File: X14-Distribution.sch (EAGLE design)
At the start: 57 parts, among them Q1 310mA/60V/1.6Ω, Q2 IRF1018EPBF, Q3 IRF1018EPBF, Q4 IRF1018EPBF, Q5 310mA/60V/1.6Ω, Q6 310mA/60V/1.6Ω, Q7 310mA/60V/1.6Ω, Q8 310mA/60V/1.6Ω, U1 DIST_OR_CONTROL_ALTMK06A-M, U2 DIST_OR_CONTROL_ALTMK06A-M

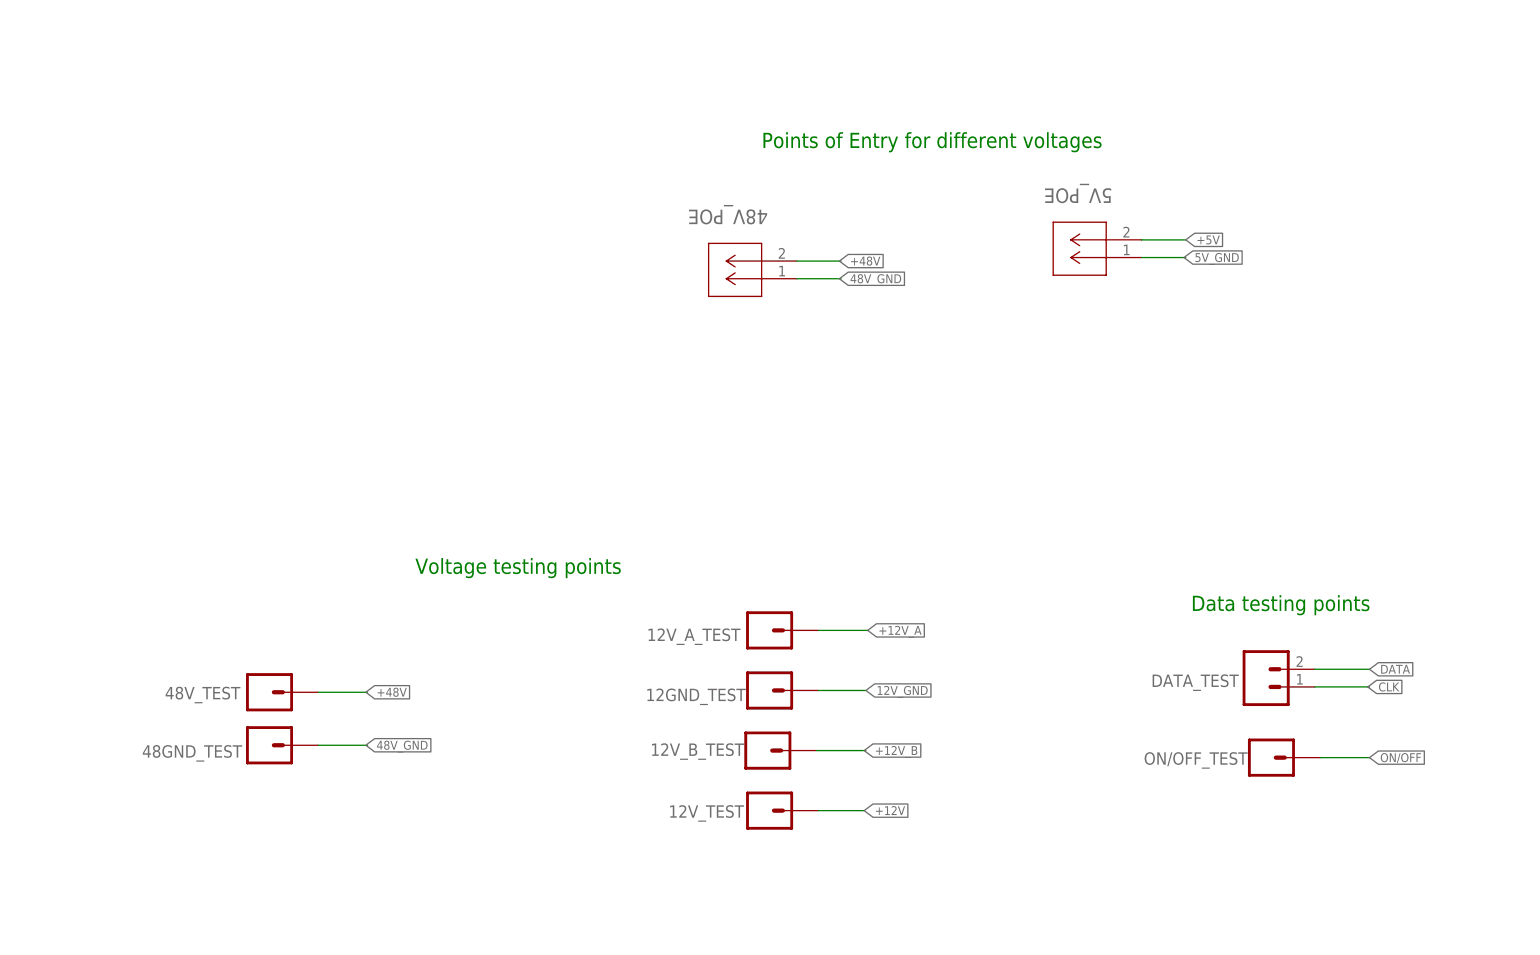
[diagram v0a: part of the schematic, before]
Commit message: Changed footprint of schottky diode
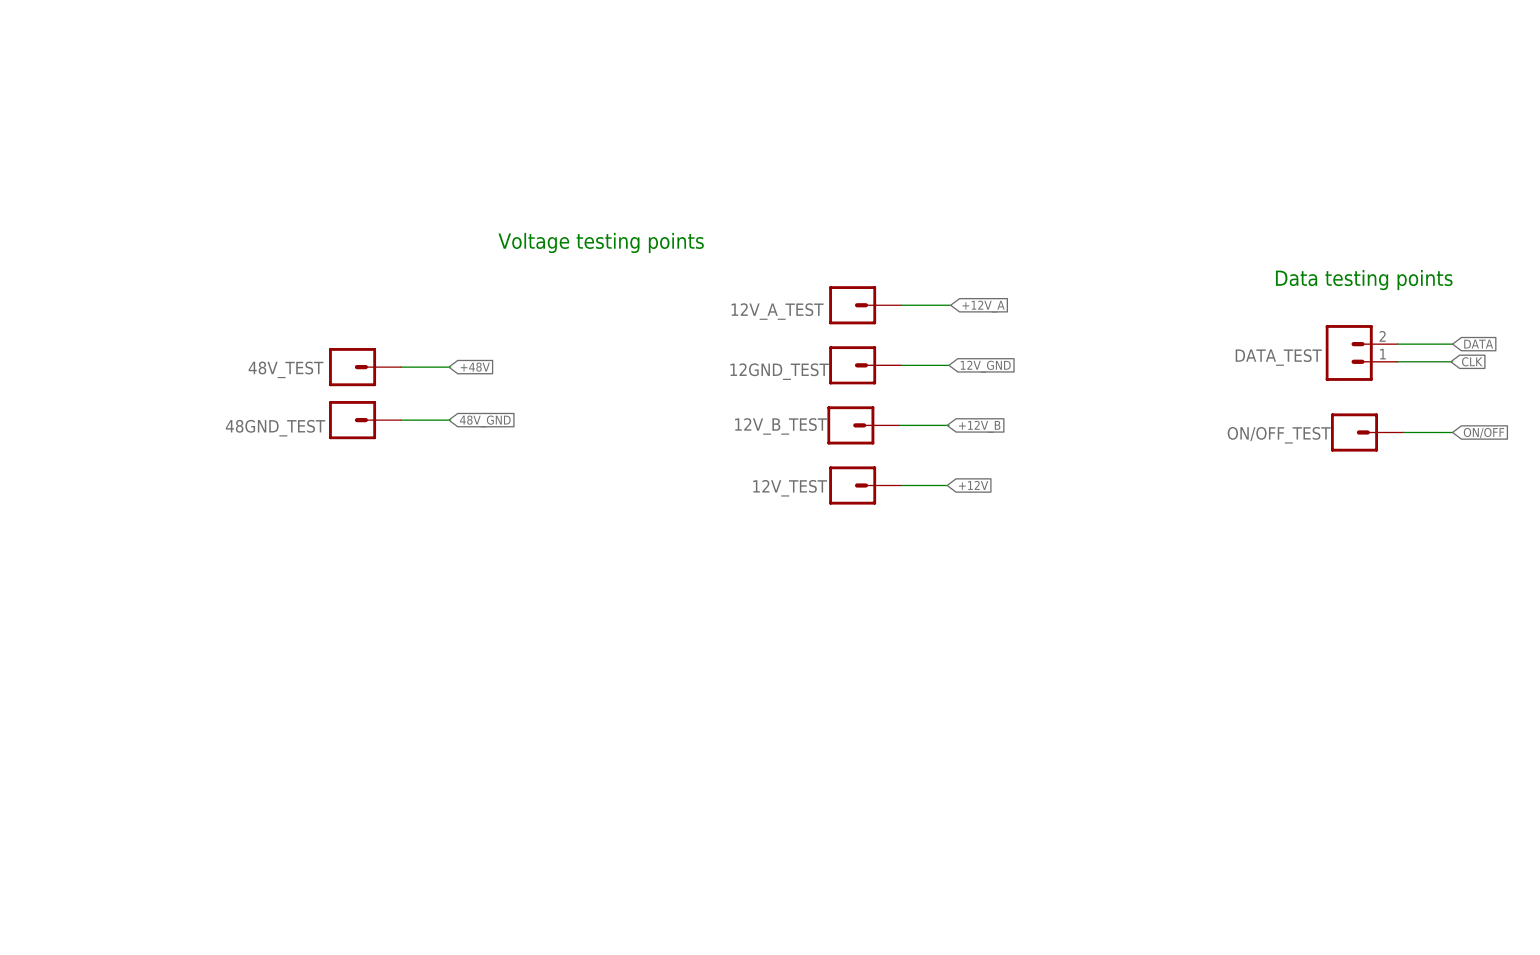
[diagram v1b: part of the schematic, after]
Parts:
- removed 48V_POE, 5V_POE: POE_TERMINAL, CONN, 2 pin screw terminal:POE_TERMINAL
- D11, D12: device DIODE, Oring Schottky Diode:DIODE-DO-214AC(SK34ATR) -> DIODE, Dist Oring Schottky Diode:DIODE-DO-214AC(SK34ATR)
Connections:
- net +48V: no longer 48V_POE.2
- net +5V: no longer 5V_POE.2
- net 48V_GND: no longer 48V_POE.1
- net 5V_GND: no longer 5V_POE.1
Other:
- note removed: "Points of Entry for different voltages"
- moved on the sheet: 12GND_TEST, 12V_A_TEST, 12V_B_TEST, 12V_TEST, 48GND_TEST, 48V_TEST, DATA_TEST, ON/OFF_TEST

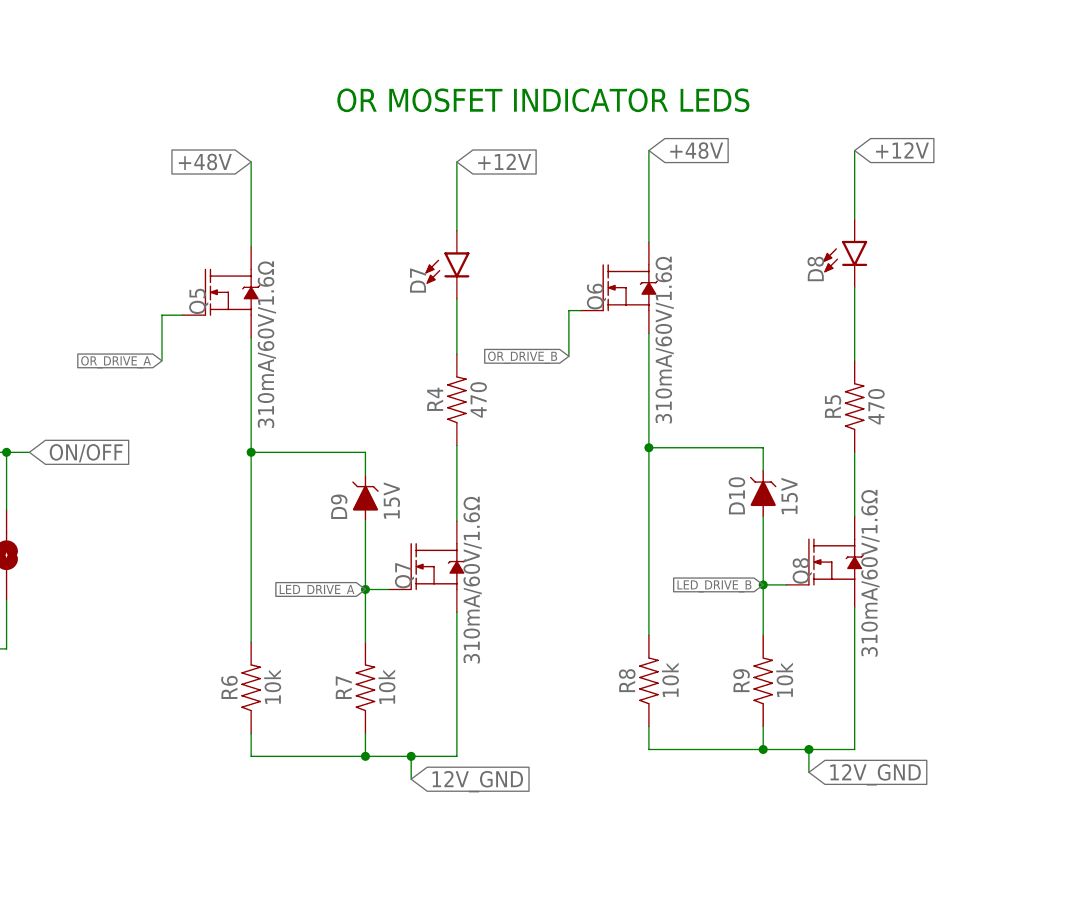
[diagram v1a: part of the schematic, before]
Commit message: Changed ORing LED MOSFETs to p-channel TSM2309CX RFG
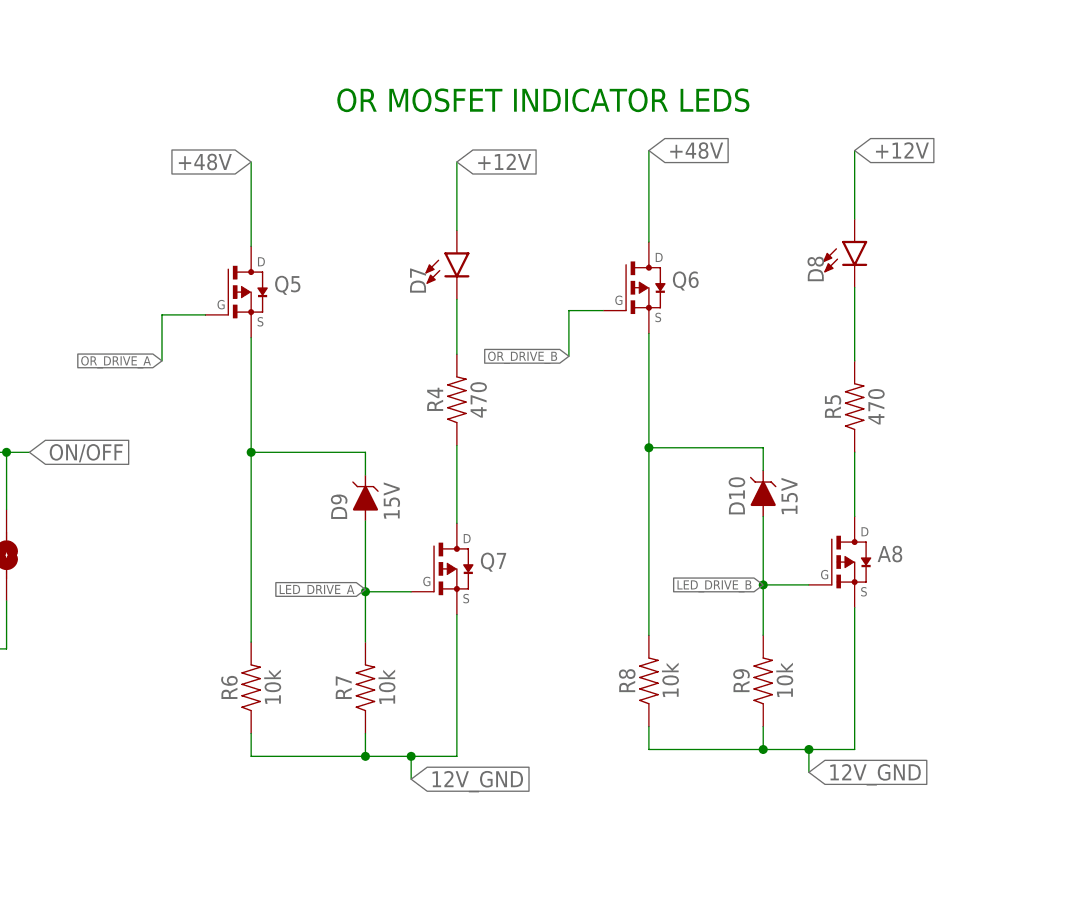
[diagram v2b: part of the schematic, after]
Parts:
- removed Q8: 310mA/60V/1.6Ω, SparkFun-DiscreteSemi:MOSFET-NCH-2N7002PW
- added A8: TRANSISTOR-FET_DMP2004K, 52101-101-REV-A_v16:TRANSISTOR-FET_DMP2004K
- Q5, Q6, Q7: value 310mA/60V/1.6Ω -> TRANSISTOR-FET_DMP2004K; device SparkFun-DiscreteSemi:MOSFET-NCH-2N7002PW -> 52101-101-REV-A_v16:TRANSISTOR-FET_DMP2004K
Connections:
- removed net N$14: Q8.D, R5.1
- new net N$7: A8.D, R5.1
- net 12V_GND: now also A8.S; no longer Q8.S
- net LED_DRIVE_B: now also A8.G; no longer Q8.G
